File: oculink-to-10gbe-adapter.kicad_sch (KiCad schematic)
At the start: 5 parts

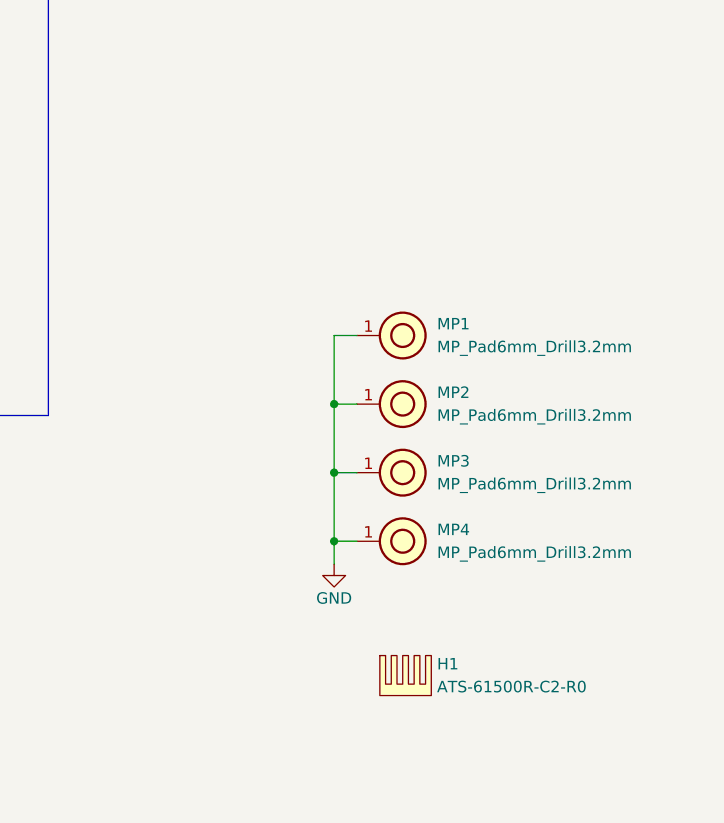
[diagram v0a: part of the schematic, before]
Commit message: [#86851] Add fan controller
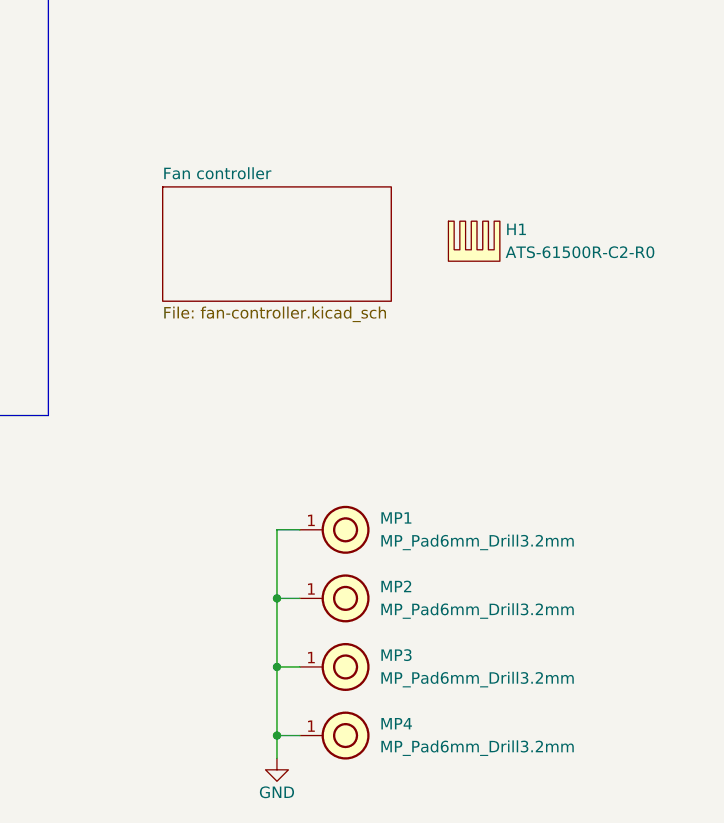
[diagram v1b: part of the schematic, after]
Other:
- added sheet Fan controller (fan-controller.kicad_sch)
- moved on the sheet: H1, MP1, MP2, MP3, MP4

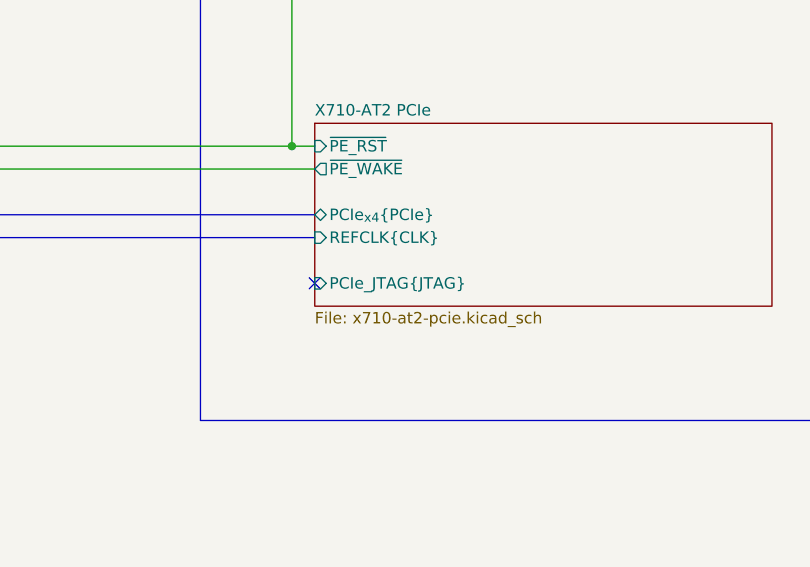
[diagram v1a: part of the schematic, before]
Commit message: [#86351] Connect Tag Connect 3V3 pin, clear ERC
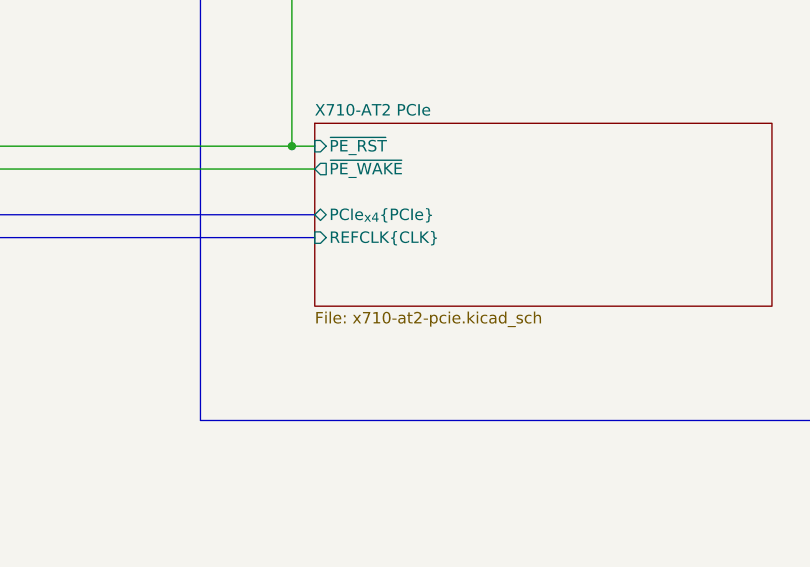
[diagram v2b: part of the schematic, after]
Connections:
- no-connect marks 1 -> 0
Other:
- sheet X710-AT2 PCIe ports: added none; removed PCIe_JTAG{JTAG}
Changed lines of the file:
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@@
 		(color 0 0 0 0)
-	)
-	(no_connect
-		(at 152.4 175.26)
 	)
 	(wire
@@
 			)
 		)
-		(pin "PCIe_JTAG{JTAG}" input
-			(at 152.4 175.26 180)
-			(effects
-				(font
-					(size 1.27 1.27)
-				)
-				(justify left)
-			)
-		)

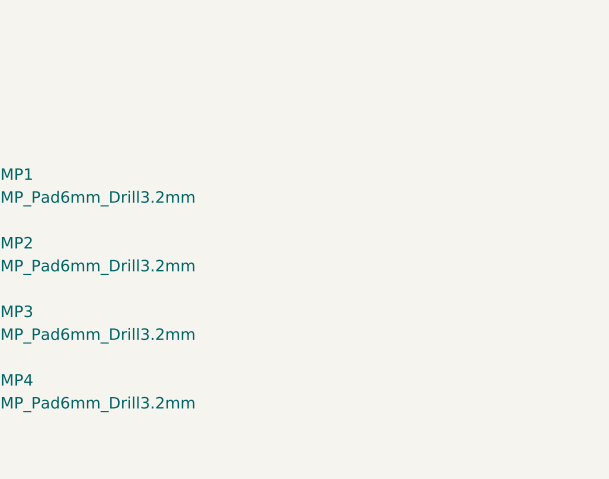
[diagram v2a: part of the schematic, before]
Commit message: [#88407] Add mounting holes with copper for the heat sink mounting screws
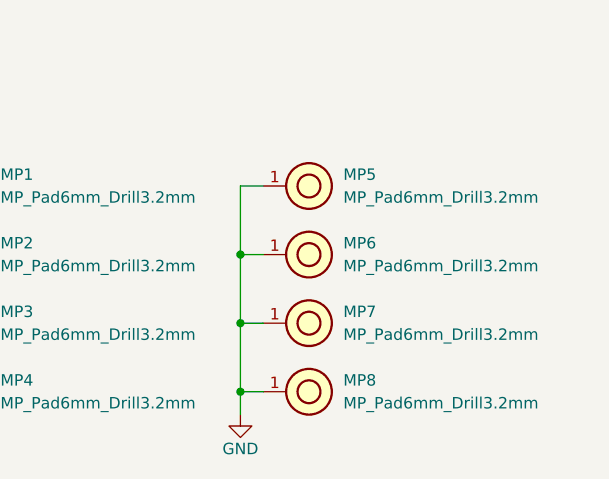
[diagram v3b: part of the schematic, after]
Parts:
- added MP5, MP6, MP7, MP8: MP_Pad6mm_Drill3.2mm, antmicro-footprints:MP_Pad6mm_Drill3.2mm, symbol antmicroMechanicalParts:MP_Pad6mm_Drill3.2mm
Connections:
- net GND: now also MP5.1, MP6.1, MP7.1, MP8.1
